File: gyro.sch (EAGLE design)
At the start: 9 parts, among them IC2 LGD20H

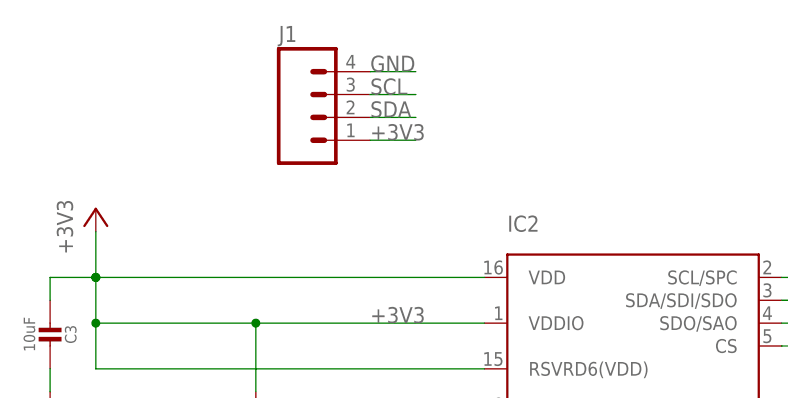
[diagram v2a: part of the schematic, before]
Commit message: added six pin header to stack with accell
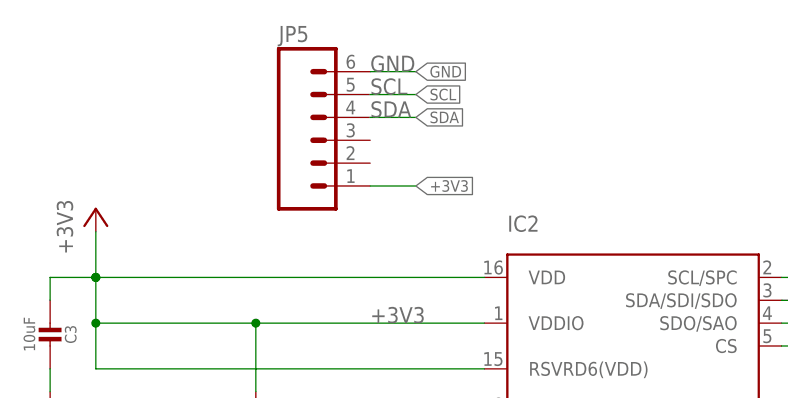
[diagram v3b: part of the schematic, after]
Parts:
- removed J1: (no value), SparkFun-Connectors:M04PTH
- added JP5: (no value), SparkFun:M06SIP
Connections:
- net +3V3: now also JP5.1; no longer J1.1
- net GND: now also JP5.6; no longer J1.4
- net SCL: now also JP5.5; no longer J1.3
- net SDA: now also JP5.4; no longer J1.2
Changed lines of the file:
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@@
 <setting verticaltext="up"/>
 </settings>
-<grid distance="0.1" unitdist="inch" unit="inch" style="lines" multiple="1" display="no" altdistance="0.01" altunitdist="inch" altunit="inch"/>
+<grid distance="0.1" unitdist="inch" unit="inch" style="lines" multiple="1" display="yes" altdistance="0.01" altunitdist="inch" altunit="inch"/>
 <layers>
 <layer number="1" name="Top" color="4" fill="1" visible="no" active="no"/>
@@
 <part name="+3V9" library="supply1" deviceset="+3V3" device=""/>
 <part name="IC2" library="microbuilder" deviceset="GYRO_L3GD20H" device="" value="LGD20H"/>
-<part name="J1" library="SparkFun-Connectors" deviceset="M04" device="PTH"/>
+<part name="JP5" library="SparkFun" deviceset="M06" device="SIP"/>
 </parts>
 <sheets>
@@
 <instance part="+3V9" gate="G$1" x="114.3" y="30.48" rot="R180"/>
 <instance part="IC2" gate="G$1" x="71.12" y="35.56"/>
-<instance part="J1" gate="G$1" x="35.56" y="71.12"/>
+<instance part="JP5" gate="G$1" x="35.56" y="68.58"/>
 </instances>
 <busses>
@@
 <wire x1="45.72" y1="76.2" x2="40.64" y2="76.2" width="0.1524" layer="91"/>
 <label x="40.64" y="76.2" size="1.778" layer="95"/>
-<pinref part="J1" gate="G$1" pin="4"/>
+<pinref part="JP5" gate="G$1" pin="6"/>
+<label x="45.72" y="76.2" size="1.27" layer="95" xref="yes"/>
 </segment>
 </net>
@@
 </segment>
 <segment>
-<wire x1="40.64" y1="68.58" x2="45.72" y2="68.58" width="0.1524" layer="91"/>
-<label x="40.64" y="68.58" size="1.778" layer="95"/>
-<pinref part="J1" gate="G$1" pin="1"/>
+<pinref part="JP5" gate="G$1" pin="1"/>
+<wire x1="40.64" y1="63.5" x2="45.72" y2="63.5" width="0.1524" layer="91"/>
+<label x="45.72" y="63.5" size="1.27" layer="95" xref="yes"/>
 </segment>
 </net>
@@
 <wire x1="40.64" y1="71.12" x2="45.72" y2="71.12" width="0.1524" layer="91"/>
 <label x="40.64" y="71.12" size="1.778" layer="95"/>
-<pinref part="J1" gate="G$1" pin="2"/>
+<pinref part="JP5" gate="G$1" pin="4"/>
+<label x="45.72" y="71.12" size="1.27" layer="95" xref="yes"/>
 </segment>
 </net>
@@
 <wire x1="40.64" y1="73.66" x2="45.72" y2="73.66" width="0.1524" layer="91"/>
 <label x="40.64" y="73.66" size="1.778" layer="95"/>
-<pinref part="J1" gate="G$1" pin="3"/>
-</segment>
-</net>
+<pinref part="JP5" gate="G$1" pin="5"/>
+<label x="45.72" y="73.66" size="1.27" layer="95" xref="yes"/>
+</segment>
+</net>

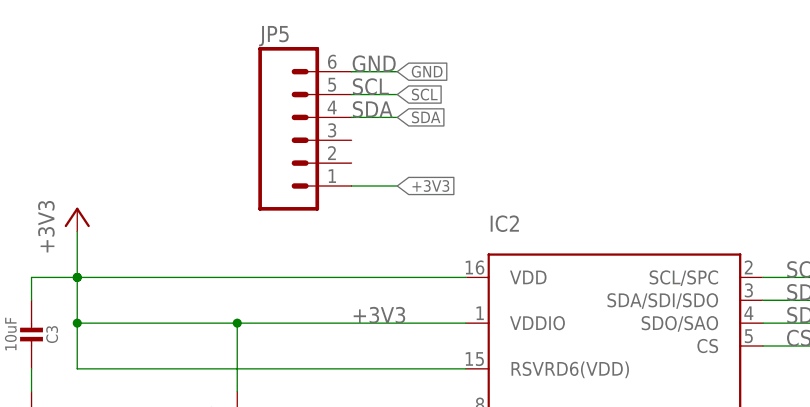
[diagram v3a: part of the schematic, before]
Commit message: set up pins to line up with accel corectly
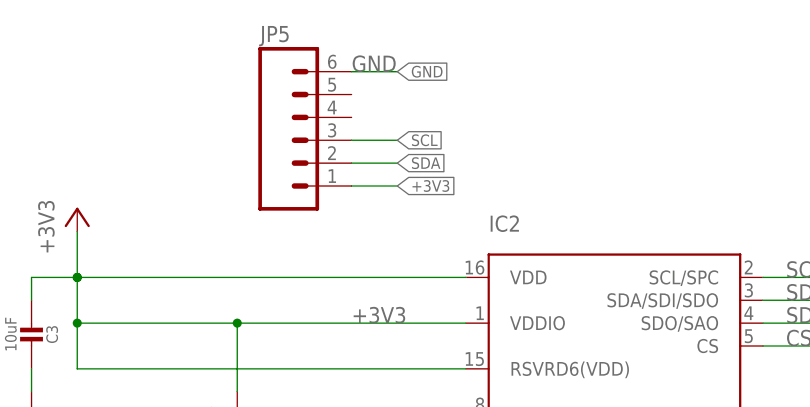
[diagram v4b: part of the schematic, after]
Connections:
- net SCL: now also JP5.3; no longer JP5.5
- net SDA: now also JP5.2; no longer JP5.4
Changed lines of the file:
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@@
 </segment>
 <segment>
-<wire x1="40.64" y1="71.12" x2="45.72" y2="71.12" width="0.1524" layer="91"/>
-<label x="40.64" y="71.12" size="1.778" layer="95"/>
-<pinref part="JP5" gate="G$1" pin="4"/>
-<label x="45.72" y="71.12" size="1.27" layer="95" xref="yes"/>
+<pinref part="JP5" gate="G$1" pin="2"/>
+<wire x1="40.64" y1="66.04" x2="45.72" y2="66.04" width="0.1524" layer="91"/>
+<label x="45.72" y="66.04" size="1.27" layer="95" xref="yes"/>
 </segment>
 </net>
@@
 </segment>
 <segment>
-<wire x1="40.64" y1="73.66" x2="45.72" y2="73.66" width="0.1524" layer="91"/>
-<label x="40.64" y="73.66" size="1.778" layer="95"/>
-<pinref part="JP5" gate="G$1" pin="5"/>
-<label x="45.72" y="73.66" size="1.27" layer="95" xref="yes"/>
+<pinref part="JP5" gate="G$1" pin="3"/>
+<wire x1="40.64" y1="68.58" x2="45.72" y2="68.58" width="0.1524" layer="91"/>
+<label x="45.72" y="68.58" size="1.27" layer="95" xref="yes"/>
 </segment>
 </net>
